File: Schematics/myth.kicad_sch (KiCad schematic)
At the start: 140 parts, among them J1 Conn_01x08_Male, J10 Conn_01x04_Male, J11 Conn_02x01, J2 Conn_01x08_Male, J3 Conn_01x08_Male, J4 Conn_01x08_Male, J5 Conn_01x08_Male, J6 Conn_01x08_Male, J8 Conn_01x08_Male, J9 Conn_01x04_Male, U1 74AHC02, U10 74HC595, U11 74HC165, U12 74AHC08, U13 74HC238, U14 74HC238, U15 74HC238, U16 4002, U17 74HC32, U18 74AHC273, U19 74LS32, U2 74AHC273, U20 CD4532BE, U21 74AHC138, U22 74AHC04, U23 74AHC138, U24 74HC238, U25 74HC238, U26 74LS32, U27 4078, U28 74AHC244, U29 74AHC138, U3 74HC74, U30 74AHC138, U31 4075, U32 74AHC02, U33 74AHC138, U34 74HC238, U35 74AHC138, U36 74HC163, U37 74AHC574, U38 74HC238, U39 74HC32, U4 74AHC04, U40 74AHC04, U41 74AHC574, U42 74HC74, U43 74AHC273, U44 74HC283, U45 74HC283, U46 74AHC273, U47 74HC02, U48 74HC157, U49 74HC157, U5 74AHC04, U50 74AHC244, U51 74AHC04, U52 74HC283, U53 74HC193, U54 74HC193, U55 74HC193, U56 74HC193, U57 74AHC273, U58 74HC193, U59 74HC193, U6 74AHC08, U60 74AHC244, U61 74LS32, U62 4078, U63 74LS08, U64 74LS21, U65 74AHC04, U66 74AHC273, U67 74HC157, U68 74HC157, U69 74AHC574, U7 74HC00, U70 74HC157, U71 74LS257, U72 74LS257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

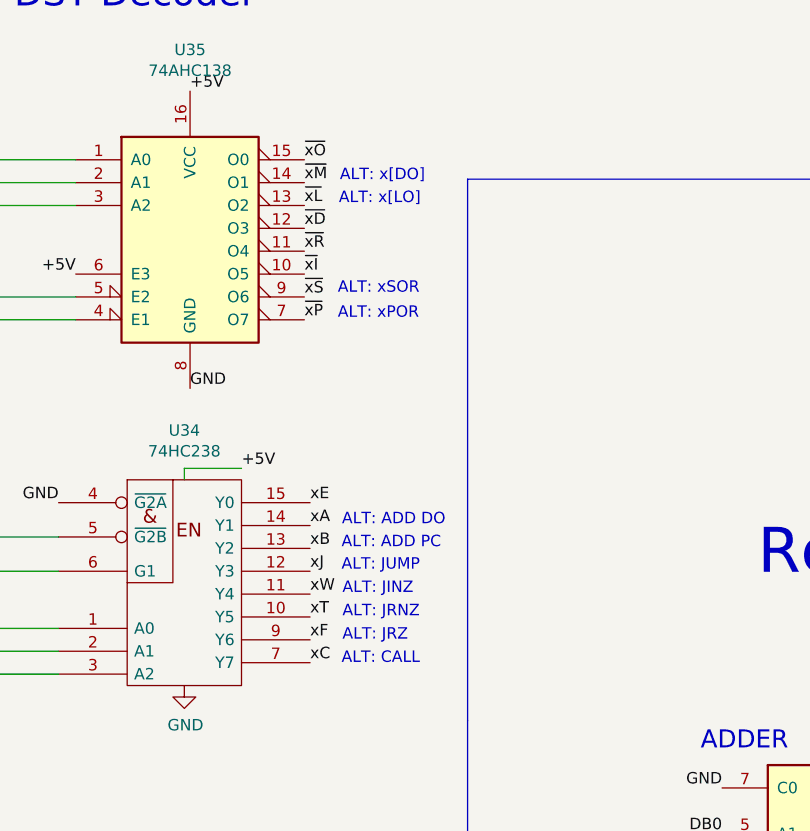
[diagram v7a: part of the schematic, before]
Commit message: Add slightly revised schematics
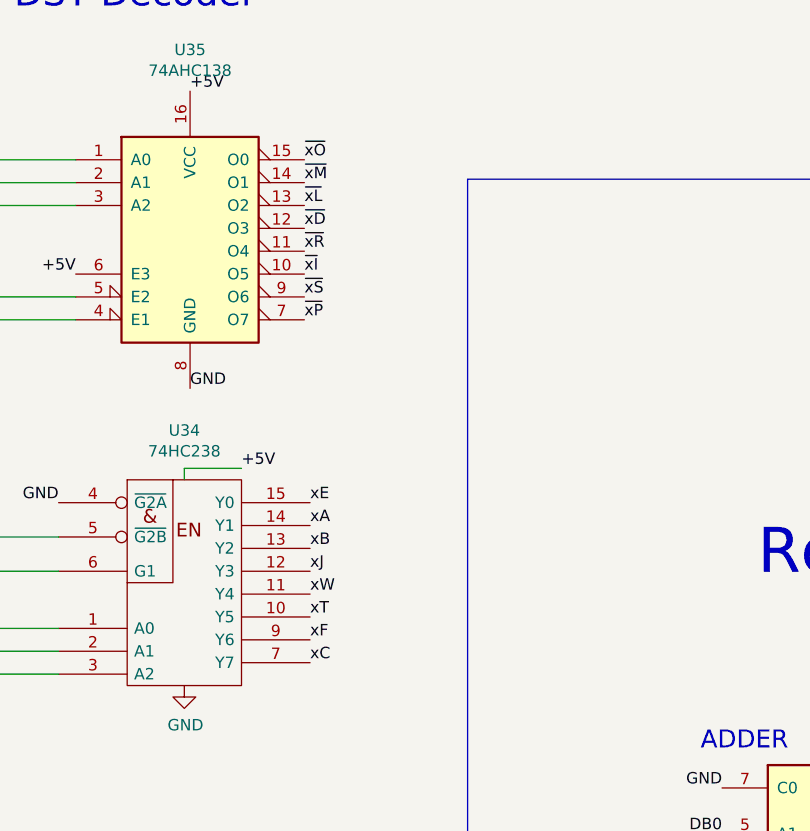
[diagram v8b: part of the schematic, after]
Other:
- note removed: "ALT: ADD DO"
- note removed: "ALT: ADD PC"
- note removed: "ALT: CALL"
- note removed: "ALT: JINZ"
- note removed: "ALT: JRNZ"
- note removed: "ALT: JRZ"
- note removed: "ALT: JUMP"
- note removed: "ALT: xPOR"
- note removed: "ALT: xSOR"
- note removed: "ALT: x[DO]"
- note removed: "ALT: x[LO]"
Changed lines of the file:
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@@
-		)
-	)
-	(text "ALT: JRNZ"
-		(exclude_from_sim no)
-		(at 368.5148 314.8425 0)
-		(effects
-			(font
-				(size 1.27 1.27)
-			)
-			(justify left bottom)
 		)
 	)
@@
 		)
 	)
-	(text "ALT: xSOR"
-		(exclude_from_sim no)
-		(at 367.9979 278.8966 0)
-		(effects
-			(font
-				(size 1.27 1.27)
-			)
-			(justify left bottom)
-		)
-	)
 	(text "Pair SRC Decoder"
 		(exclude_from_sim no)
@@
 		)
 	)
-	(text "ALT: ADD PC"
-		(exclude_from_sim no)
-		(at 368.4151 307.1688 0)
-		(effects
-			(font
-				(size 1.27 1.27)
-			)
-			(justify left bottom)
-		)
-	)
 	(text "W=While\nIntended to\npost decrement\nfor either case"
 		(exclude_from_sim no)
@@
 		(exclude_from_sim no)
 		(at 890.6394 594.821 0)
-		(effects
-			(font
-				(size 1.27 1.27)
-			)
-			(justify left bottom)
-		)
-	)
-	(text "ALT: xPOR"
-		(exclude_from_sim no)
-		(at 367.9979 281.6772 0)
 		(effects
 			(font
@@
 		)
 	)
-	(text "ALT: x[DO]"
-		(exclude_from_sim no)
-		(at 368.2296 266.384 0)
-		(effects
-			(font
-				(size 1.27 1.27)
-			)
-			(justify left bottom)
-		)
-	)
 	(text "Branching"
 		(exclude_from_sim no)
@@
 		)
 	)
-	(text "ALT: CALL"
-		(exclude_from_sim no)
-		(at 368.4151 320.0247 0)
-		(effects
-			(font
-				(size 1.27 1.27)
-			)
-			(justify left bottom)
-		)
-	)
 	(text "~{RES} request"
 		(exclude_from_sim no)
@@
 		)
 	)
-	(text "ALT: JUMP"
-		(exclude_from_sim no)
-		(at 368.4151 309.6603 0)
-		(effects
-			(font
-				(size 1.27 1.27)
-			)
-			(justify left bottom)
-		)
-	)
 	(text "Hard-coded:\nif bits 0-2 all 0\nreplace by 4"
 		(exclude_from_sim no)
@@
 		)
 	)
-	(text "ALT: x[LO]"
-		(exclude_from_sim no)
-		(at 368.1137 268.9328 0)
-		(effects
-			(font
-				(size 1.27 1.27)
-			)
-			(justify left bottom)
-		)
-	)
 	(text "Power"
 		(exclude_from_sim no)
@@
 		)
 	)
-	(text "ALT: ADD DO"
-		(exclude_from_sim no)
-		(at 368.4613 304.6169 0)
-		(effects
-			(font
-				(size 1.27 1.27)
-			)
-			(justify left bottom)
-		)
-	)
-	(text "ALT: JINZ"
-		(exclude_from_sim no)
-		(at 368.5148 312.2514 0)
-		(effects
-			(font
-				(size 1.27 1.27)
-			)
-			(justify left bottom)
-		)
-	)
 	(text " 8 AND (R:=R&O)\n 9 IOR (R:=R|O)\n10 EOR (R:=R^O)\n11 ADD (Add\" / R:=R+O, bits 0-7)\n12 CAR (\"Carry Bit\" / R:= Carry, 9th bit of R+O) 00h or 01h\n13 RLO (\"Flag: R less than O\" / R:= (R<O)? 0xFF:0\n14 REO (\"Flag: R equals O\" / R:= (R==O)? 0xFF:0\n15 RGO (\"Flag: R greater than O\" / R:= (R>O)? 0xFF:0\n"
 		(exclude_from_sim no)
@@
 			)
 			(justify left bottom)
-		)
-	)
-	(text "ALT: JRZ"
-		(exclude_from_sim no)
-		(at 368.5148 317.4336 0)
-		(effects
-			(font
-				(size 1.27 1.27)
-			)
-			(justify left bottom)
